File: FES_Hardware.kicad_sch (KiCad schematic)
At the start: 0 parts

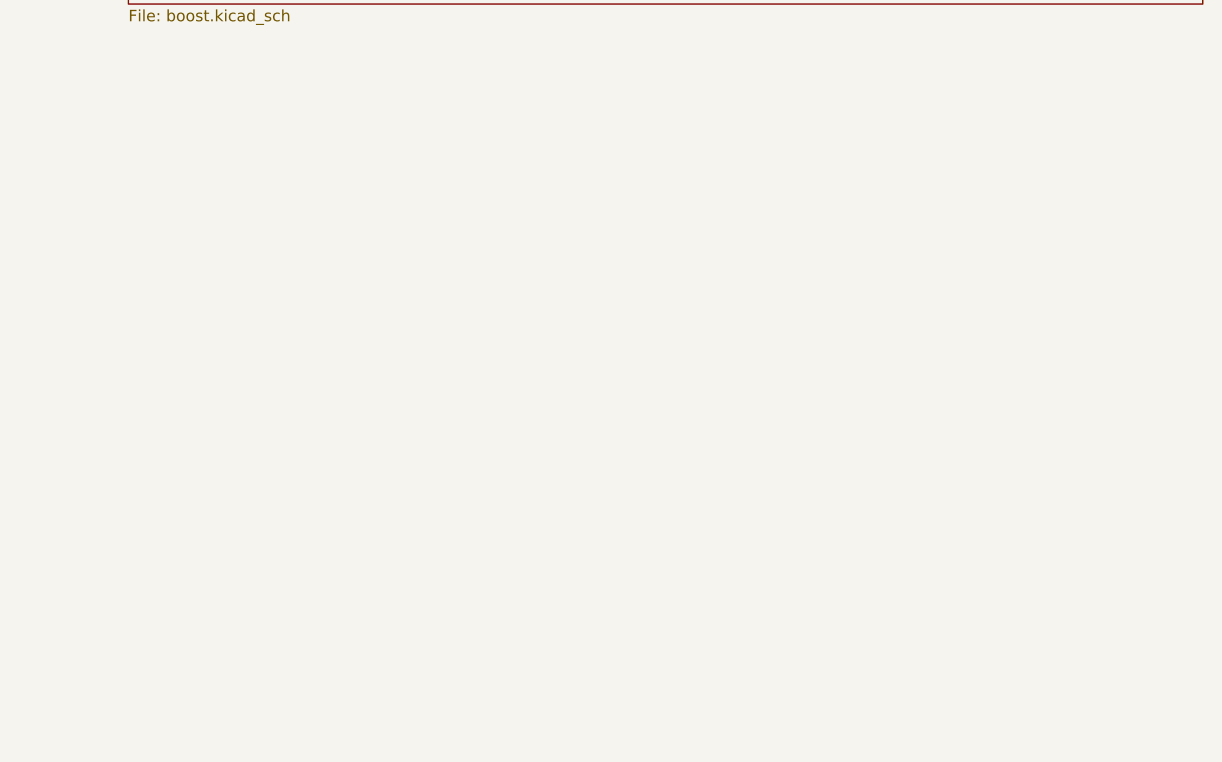
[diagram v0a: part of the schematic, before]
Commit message: Added H-Bridge, completed HV schematic
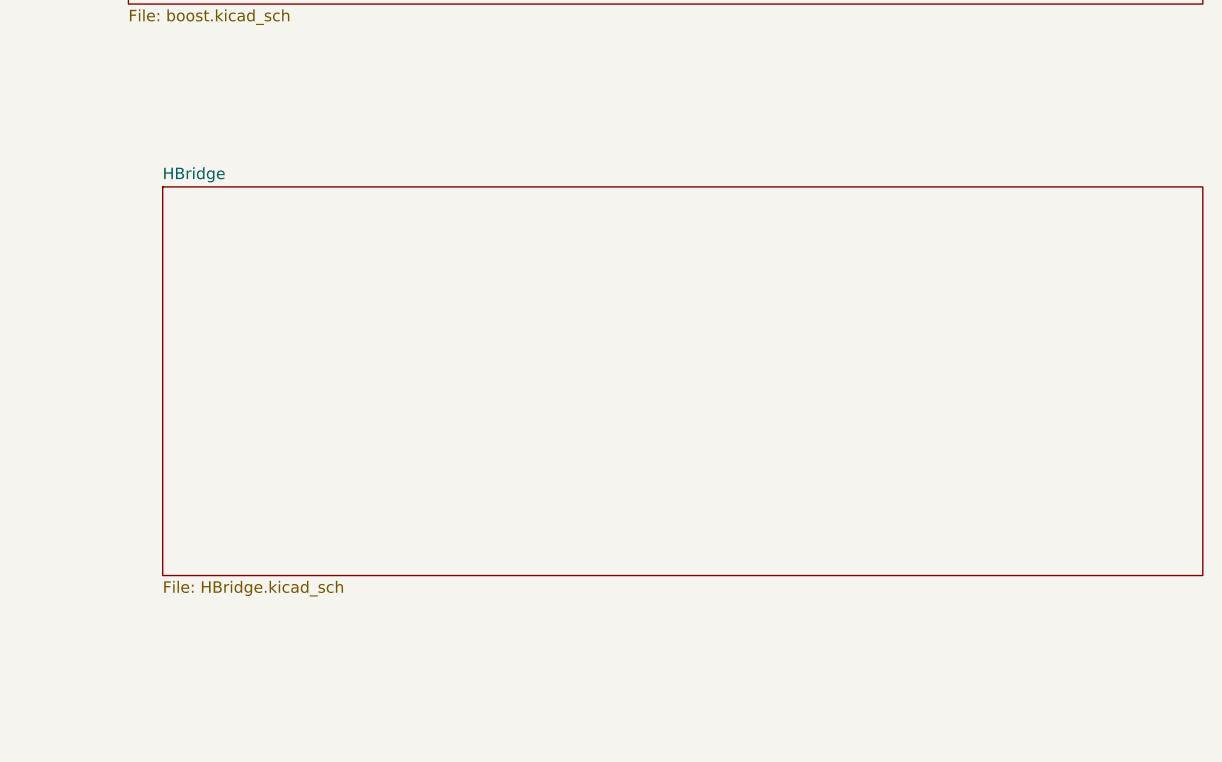
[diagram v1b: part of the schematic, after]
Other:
- added sheet HBridge (HBridge.kicad_sch)
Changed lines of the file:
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@@
+	)
+	(sheet
+		(at 158.75 116.84)
+		(size 115.57 43.18)
+		(fields_autoplaced yes)
+		(stroke
+			(width 0.1524)
+			(type solid)
+		)
+		(fill
+			(color 0 0 0 0.0000)
+		)
+		(property "Sheetname" "HBridge"
+			(at 158.75 116.1284 0)
+			(effects
+				(font
+					(size 1.27 1.27)
+				)
+				(justify left bottom)
+			)
+		)
+		(property "Sheetfile" "HBridge.kicad_sch"
+			(at 158.75 160.6046 0)
+			(effects
+				(font
+					(size 1.27 1.27)
+				)
+				(justify left top)
+			)
+		)
+		(instances
+			(project "FES_Hardware"
+				(path "/225cfa82-97e7-4320-90e1-4d94ef39f9f2"
+					(page "5")
+				)
+			)
+		)
 	)
 	(sheet
